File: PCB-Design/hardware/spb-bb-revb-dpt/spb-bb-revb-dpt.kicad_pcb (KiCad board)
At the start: 4 copper layers, 89.5 x 85.2 mm, 191 parts, among them J1 DC+, J10 U.FL L2, J11 U.FL D2, J12 V_ISO,HS in: 1 +, 2 -, J13 V_ISO,LS in: 1 +, 2 -, J14 CTRL2: 1 RTN 2 PWMH 3 RTN 4 P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, J15 U.FL H3, J16 U.FL L3, J17 U.FL D3, J18 U.FL H4, J19 U.FL L4, J2 DC-, J20 U.FL D4, J21 AC, J3 V_ISO,HS in: 1 +, 2 -, J4 V_ISO,LS in: 1 +, 2 -, J5 CTRL1: 1 RTN 2 PWMH 3 RTN 4 P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, J6 U.FL H1, J7 U.FL L1, J8 U.FL D1, J9 U.FL H2, Q1 EPC2361, Q2 EPC2361, Q3 EPC2361, Q4 EPC2361, Q5 EPC2361, Q6 EPC2361, Q7 EPC2361, Q8 EPC2361, U1 2EDF7275K, U2 2EDF7275K

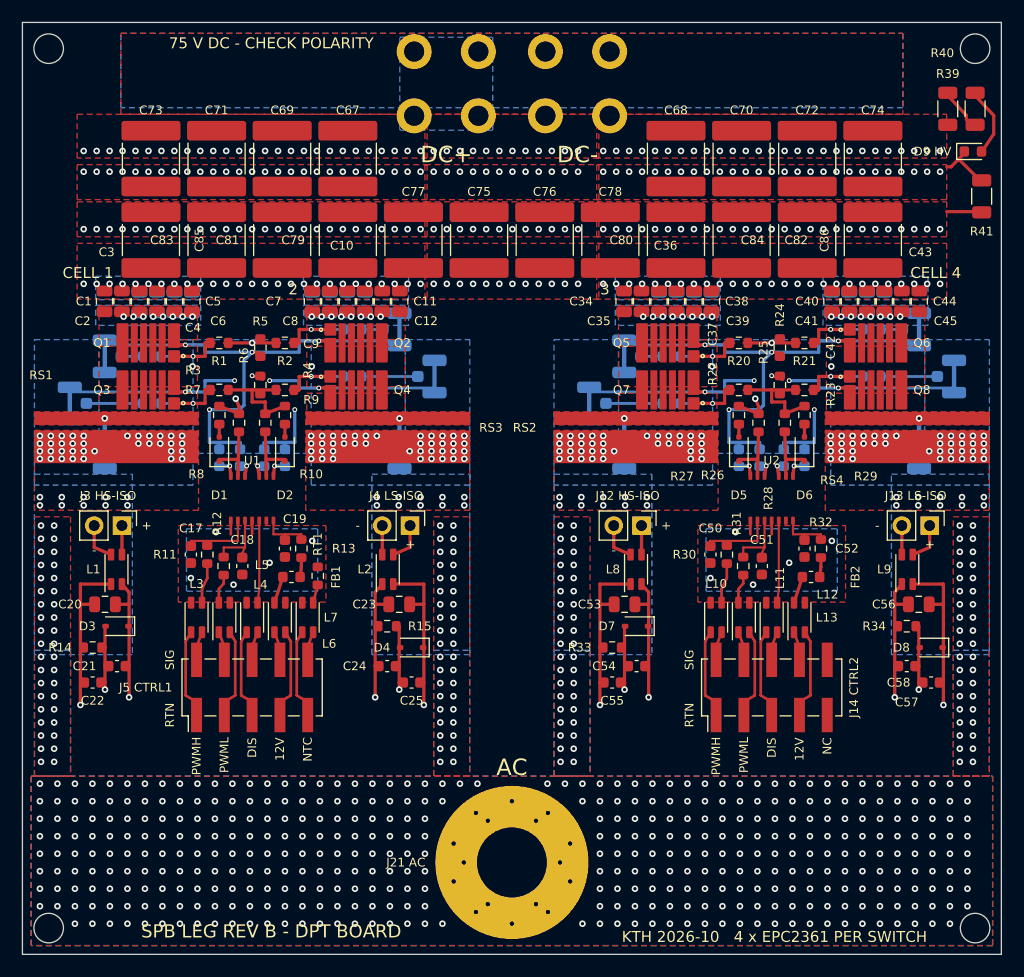
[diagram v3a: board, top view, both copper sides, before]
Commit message: DPT board: review fixes - MMCX V_DS ports, saved project rules, test points
Fixes from reports/pcb-rules/spb-bb-revb-dpt-review-2026-10-19.md (DPT only):
- V_DS ports: the U.FL (30 V rating) is replaced by Wurth WR-MMCX
  66012102111404 vertical SMT jacks (170 V rms): centre SW, shield LSRCx,
  bottom side next to each LS FET. The shield goes through the LSS via from
  the shunt IN land; ~25 DC- vias per cell are pruned (mirror pairs).
- Project rules written into the .kicad_pro (track / clearance / connection
  0.2 mm, vias 0.45 / 0.25 mm, ring 0.1 mm, mask web 0.1 mm, courtyards).
  A fresh load of the saved project: DRC 0 / 0 / 0.
- Inner planes: unused inner via rings removed and 0.25 mm minimum fill
  width (the 0.1-0.18 mm necks between antipads are gone).
- Driver barrier exception narrowed to pads and pin-escape tracks.
- Bring-up test points and spring-tip probe pads (board-only footprints,
  scripts/test_points.py, list in fab/testpoints.csv); terminal rule refs
  taken from the board; pad_nets.json written by the generator.
- Docs: DPT_measurement_setup.md, measurement slide, mechanical BOM AC ref,
  stale silk plots archived.
Schematic = PCB (0 problems). Load board not updated in this commit.

Co-Authored-By: Claude Opus 5.5 <noreply@anthropic.com>
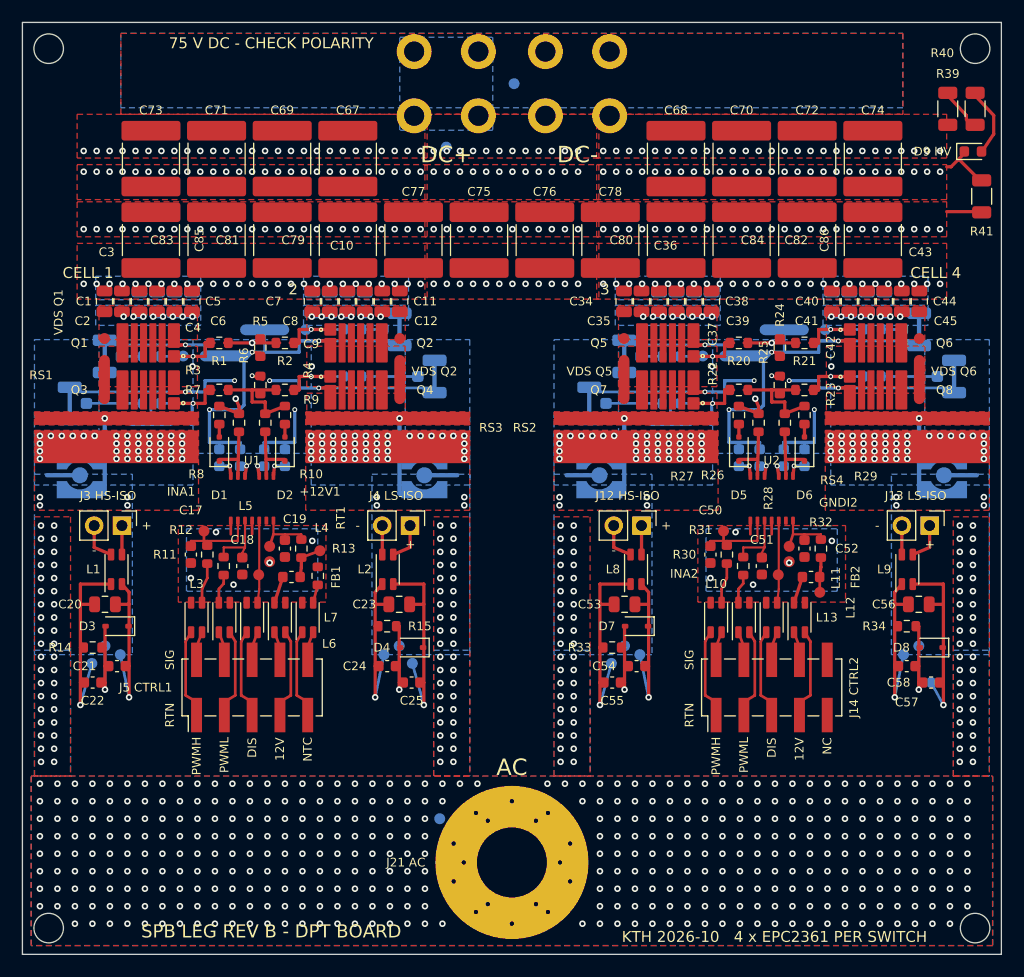
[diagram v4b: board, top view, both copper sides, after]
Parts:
- added TP1: GNDI1, spb_fab:TestPoint_Pad_D1.0mm, F.Cu at (127.8, 124.9)
- added TP11: VDDB1, spb_fab:TestPoint_Pad_D1.0mm, B.Cu at (140.9, 134.2)
- added TP12: VEEB1, spb_fab:TestPoint_Pad_D1.0mm, B.Cu at (138.3, 133.4)
- added TP13: KL1, spb_fab:TestPoint_Pad_D1.0mm, B.Cu at (139.7, 132.6)
- added TP15: VGS Q1, spb_fab:TestPoint_Spring_1.0_GND1.5-6.0, B.Cu at (120.0, 106.1)
- added TP16: VGS Q2, spb_fab:TestPoint_Spring_1.0_GND1.5-6.0, B.Cu at (131.2, 103.7)
- added TP17: VGS Q3, spb_fab:TestPoint_Spring_1.0_GND1.5-6.0, B.Cu at (120.8, 112.0)
- added TP19: GNDI2, spb_fab:TestPoint_Pad_D1.0mm, F.Cu at (175.3, 124.9)
- added TP2: +12V1, spb_fab:TestPoint_Pad_D1.0mm, F.Cu at (132.4, 123.9)
- added TP20: +12V2, spb_fab:TestPoint_Pad_D1.0mm, F.Cu at (178.2, 127.7)
- added TP21: VDDI2, spb_fab:TestPoint_Pad_D1.0mm, F.Cu at (175.3, 123.5)
- added TP22: INA2, spb_fab:TestPoint_Pad_D1.0mm, F.Cu at (169.3, 122.1)
- added TP24: DIS2, spb_fab:TestPoint_Pad_D1.0mm, F.Cu at (174.3, 126.1)
- added TP25: VDDA2, spb_fab:TestPoint_Pad_D1.0mm, B.Cu at (161.7, 133.4)
- added TP26: VEEA2, spb_fab:TestPoint_Pad_D1.0mm, B.Cu at (159.1, 134.2)
- added TP27: KH2, spb_fab:TestPoint_Pad_D1.0mm, B.Cu at (160.3, 132.6)
- added TP29: VDDB2, spb_fab:TestPoint_Pad_D1.0mm, B.Cu at (188.3, 135.9)
- added TP3: VDDI1, spb_fab:TestPoint_Pad_D1.0mm, F.Cu at (127.8, 123.5)
- added TP30: VEEB2, spb_fab:TestPoint_Pad_D1.0mm, B.Cu at (185.8, 133.4)
- added TP31: KL2, spb_fab:TestPoint_Pad_D1.0mm, B.Cu at (187.2, 132.6)
- added TP33: VGS Q5, spb_fab:TestPoint_Spring_1.0_GND1.5-6.0, B.Cu at (167.4, 106.1)
- added TP34: VGS Q6, spb_fab:TestPoint_Spring_1.0_GND1.5-6.0, B.Cu at (178.7, 103.7)
- added TP35: VGS Q7, spb_fab:TestPoint_Spring_1.0_GND1.5-6.0, B.Cu at (168.2, 112.0)
- added TP38: VDS Q1, spb_fab:TestPoint_Spring_1.0_GND1.5-6.0, F.Cu at (112.8, 104.5)
- added TP4: INA1, spb_fab:TestPoint_Pad_D1.0mm, F.Cu at (121.8, 122.1)
- added TP40: VDS Q2, spb_fab:TestPoint_Spring_1.0_GND1.5-6.0, F.Cu at (139.8, 104.5)
- added TP42: VDS Q5, spb_fab:TestPoint_Spring_1.0_GND1.5-6.0, F.Cu at (160.2, 104.5)
- added TP44: VDS Q6, spb_fab:TestPoint_Spring_1.0_GND1.5-6.0, F.Cu at (187.2, 104.5)
- added TP45: DC+, spb_fab:TestPoint_Pad_D1.0mm, B.Cu at (144.0, 87.0)
- added TP46: DC-, spb_fab:TestPoint_Pad_D1.0mm, B.Cu at (150.2, 81.2)
- added TP47: SW, spb_fab:TestPoint_Pad_D1.0mm, B.Cu at (143.4, 148.4)
- added TP6: DIS1, spb_fab:TestPoint_Pad_D1.0mm, F.Cu at (126.8, 126.1)
- added TP7: VDDA1, spb_fab:TestPoint_Pad_D1.0mm, B.Cu at (114.2, 133.4)
- added TP8: VEEA1, spb_fab:TestPoint_Pad_D1.0mm, B.Cu at (111.6, 134.2)
- added TP9: KH1, spb_fab:TestPoint_Pad_D1.0mm, B.Cu at (112.8, 132.6)
- J10: value U.FL L2 -> U.FL H2
- J11: value U.FL D2 -> U.FL L2
- J15: value U.FL H3 -> MMCX VDS L3; footprint spb_fab:U.FL_Hirose_U.FL-R-SMT-1_Vertical -> spb_fab:WR-MMCX_Wuerth_66012102111404_Vertical
- J16: value U.FL L3 -> U.FL H3
- J17: value U.FL D3 -> U.FL L3
- J18: value U.FL H4 -> MMCX VDS L4; footprint spb_fab:U.FL_Hirose_U.FL-R-SMT-1_Vertical -> spb_fab:WR-MMCX_Wuerth_66012102111404_Vertical
- J19: value U.FL L4 -> U.FL H4
- J20: value U.FL D4 -> U.FL L4
- J6: value U.FL H1 -> MMCX VDS L1; footprint spb_fab:U.FL_Hirose_U.FL-R-SMT-1_Vertical -> spb_fab:WR-MMCX_Wuerth_66012102111404_Vertical
- J7: value U.FL L1 -> U.FL H1
- J8: value U.FL D1 -> U.FL L1
- J9: value U.FL H2 -> MMCX VDS L2; footprint spb_fab:U.FL_Hirose_U.FL-R-SMT-1_Vertical -> spb_fab:WR-MMCX_Wuerth_66012102111404_Vertical
- moved J18 13.6 mm to (189.5, 117.0), turned to -90 degrees
- moved J9 13.6 mm to (142.0, 117.0), turned to -90 degrees
- moved J15 11.2 mm to (158.0, 117.0), turned to -90 degrees
- moved J6 11.2 mm to (110.5, 117.0), turned to -90 degrees
- moved J11 7.63 mm to (142.4, 108.0)
- moved J20 7.63 mm to (189.9, 108.0)
- moved J8 5.50 mm to (110.0, 110.4)
- moved J17 5.50 mm to (157.6, 110.4)
- moved J7 5.36 mm to (113.2, 106.1)
- moved J16 5.36 mm to (160.8, 106.1)
- moved J10 5.36 mm to (139.2, 103.7)
- moved J19 5.36 mm to (186.8, 103.7)
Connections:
- J10 pad 1: UFL_L2 -> UFL_H2
- J10 pad 2: KL1 -> KH1
- J11 pad 1: SW -> UFL_L2
- J11 pad 2: LSRC2 -> KL1
- J15 pad 1: UFL_H3 -> SW
- J15 pad 2: KH2 -> LSRC3
- J16 pad 1: UFL_L3 -> UFL_H3
- J16 pad 2: KL2 -> KH2
- J17 pad 1: SW -> UFL_L3
- J17 pad 2: LSRC3 -> KL2
- J18 pad 1: UFL_H4 -> SW
- J18 pad 2: KH2 -> LSRC4
- J19 pad 1: UFL_L4 -> UFL_H4
- J19 pad 2: KL2 -> KH2
- J20 pad 1: SW -> UFL_L4
- J20 pad 2: LSRC4 -> KL2
- J6 pad 1: UFL_H1 -> SW
- J6 pad 2: KH1 -> LSRC1
- J7 pad 1: UFL_L1 -> UFL_H1
- J7 pad 2: KL1 -> KH1
- J8 pad 1: SW -> UFL_L1
- J8 pad 2: LSRC1 -> KL1
- J9 pad 1: UFL_H2 -> SW
- J9 pad 2: KH1 -> LSRC2
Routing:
- net KL2: track 99.9 -> 106.5 mm
- net KL1: track 99.9 -> 106.5 mm
- net KH2: track 95.2 -> 101.6 mm
- net KH1: track 95.2 -> 101.6 mm
- net LSRC4: track 4.58 -> 9.12 mm
- net LSRC3: track 4.58 -> 9.12 mm
- net LSRC2: track 4.58 -> 9.12 mm
- net LSRC1: track 4.58 -> 9.12 mm
- net VDDA2: track 44.4 -> 48.4 mm
- net VDDA1: track 44.4 -> 48.4 mm
- net VEEB2: track 44.6 -> 48.6 mm
- net VEEB1: track 44.6 -> 48.6 mm
- net VDDB1: track 54.1 -> 58.1 mm
- net VEEA2: track 54.4 -> 58.3 mm
- net VEEA1: track 54.4 -> 58.3 mm
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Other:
- board text added: "+12V1"
- board text added: "GNDI2"
- board text added: "INA1"
- board text added: "INA2"
- board text added: "J10 VGS-H2"
- board text added: "J11 VGS-L2"
- board text added: "J15 VDS-L3"
- board text added: "J16 VGS-H3"
- board text added: "J17 VGS-L3"
- board text added: "J18 VDS-L4"
- board text added: "J19 VGS-H4"
- board text added: "J20 VGS-L4"
- board text added: "J6 VDS-L1"
- board text added: "J7 VGS-H1"
- board text added: "J8 VGS-L1"
- board text added: "J9 VDS-L2"
- board text added: "KH1"
- board text added: "KH2"
- board text added: "KL1"
- board text added: "KL2"
- board text added: "SW"
- board text added: "VDDA1"
- board text added: "VDDA2"
- board text added: "VDDB1"
- board text added: "VDDB2"
- board text added: "VDS MMCX: SW / LSRC, 75 V - RATED PROBE ONLY"
- board text added: "VDS Q1"
- board text added: "VDS Q2"
- board text added: "VDS Q5"
- board text added: "VDS Q6"
- board text added: "VEEA1"
- board text added: "VEEA2"
- board text added: "VEEB1"
- board text added: "VEEB2"
- board text added: "VGS Q1"
- board text added: "VGS Q2"
- board text added: "VGS Q3"
- board text added: "VGS Q5"
- board text added: "VGS Q6"
- board text added: "VGS Q7"
- board text removed: "J10 VGS-L2"
- board text removed: "J11 VDS-L2"
- board text removed: "J15 VGS-H3"
- board text removed: "J16 VGS-L3"
- board text removed: "J17 VDS-L3"
- board text removed: "J18 VGS-H4"
- board text removed: "J19 VGS-L4"
- board text removed: "J20 VDS-L4"
- board text removed: "J6 VGS-H1"
- board text removed: "J7 VGS-L1"
- board text removed: "J8 VDS-L1"
- board text removed: "J9 VGS-H2"
- board text removed: "VDS U.FL = 75 V: 1 MOHM SCOPE INPUT ONLY"
